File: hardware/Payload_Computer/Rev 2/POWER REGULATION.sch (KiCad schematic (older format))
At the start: 8 parts, among them U301 MIC29151-5.0WU-TR

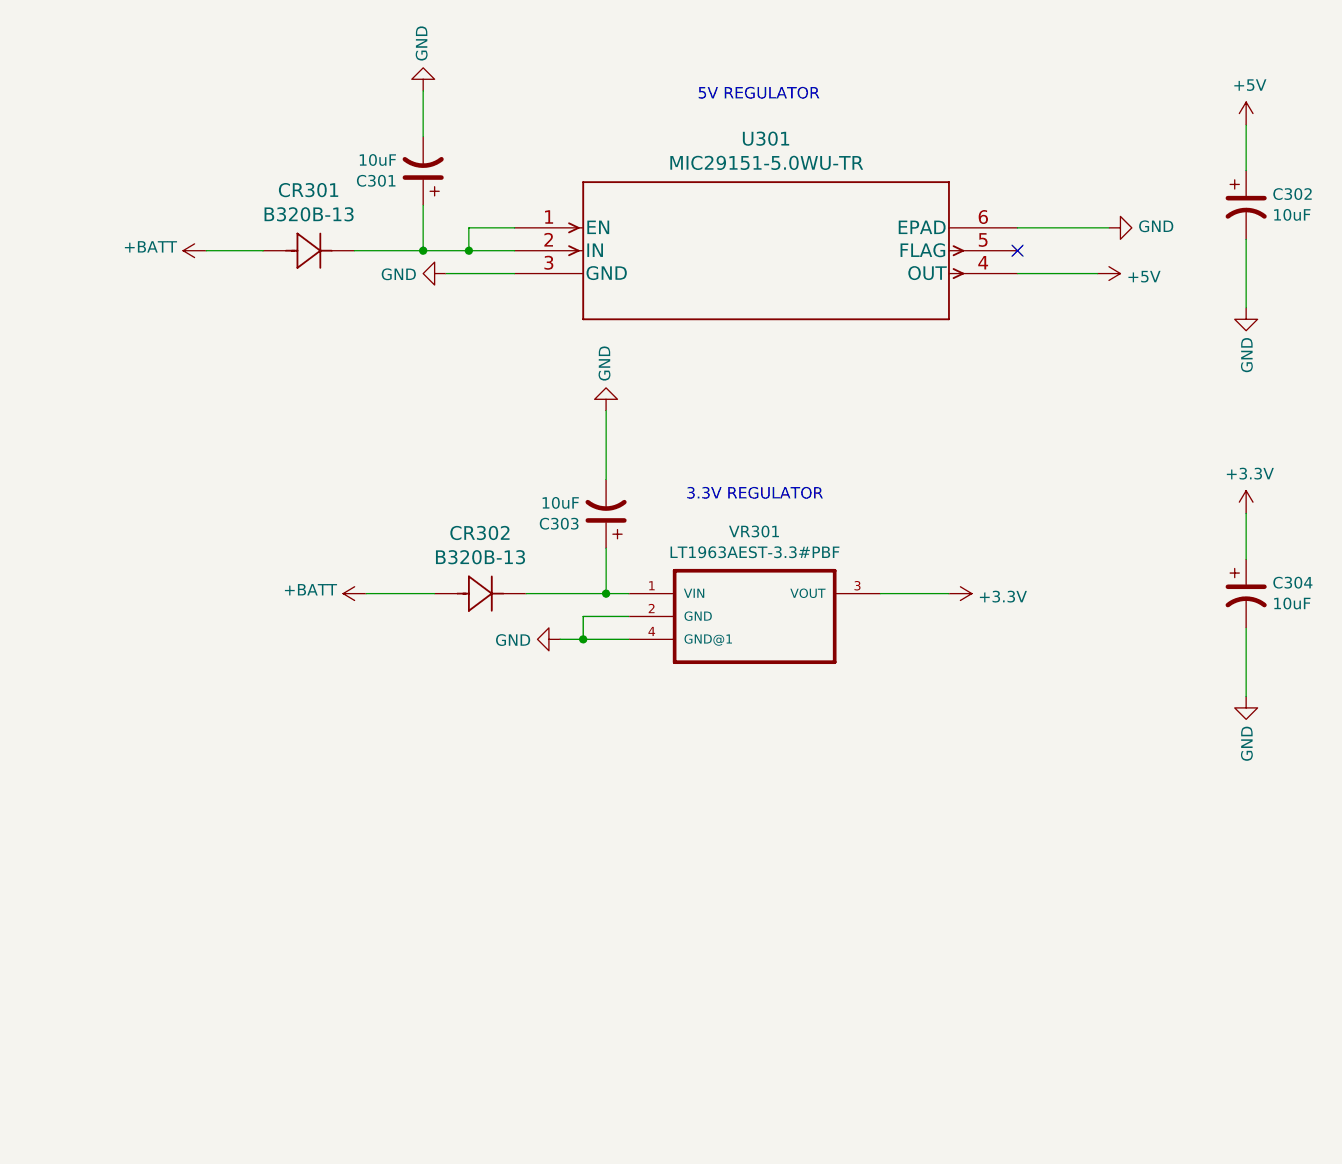
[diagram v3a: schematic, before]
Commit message: More routing and added BNO055
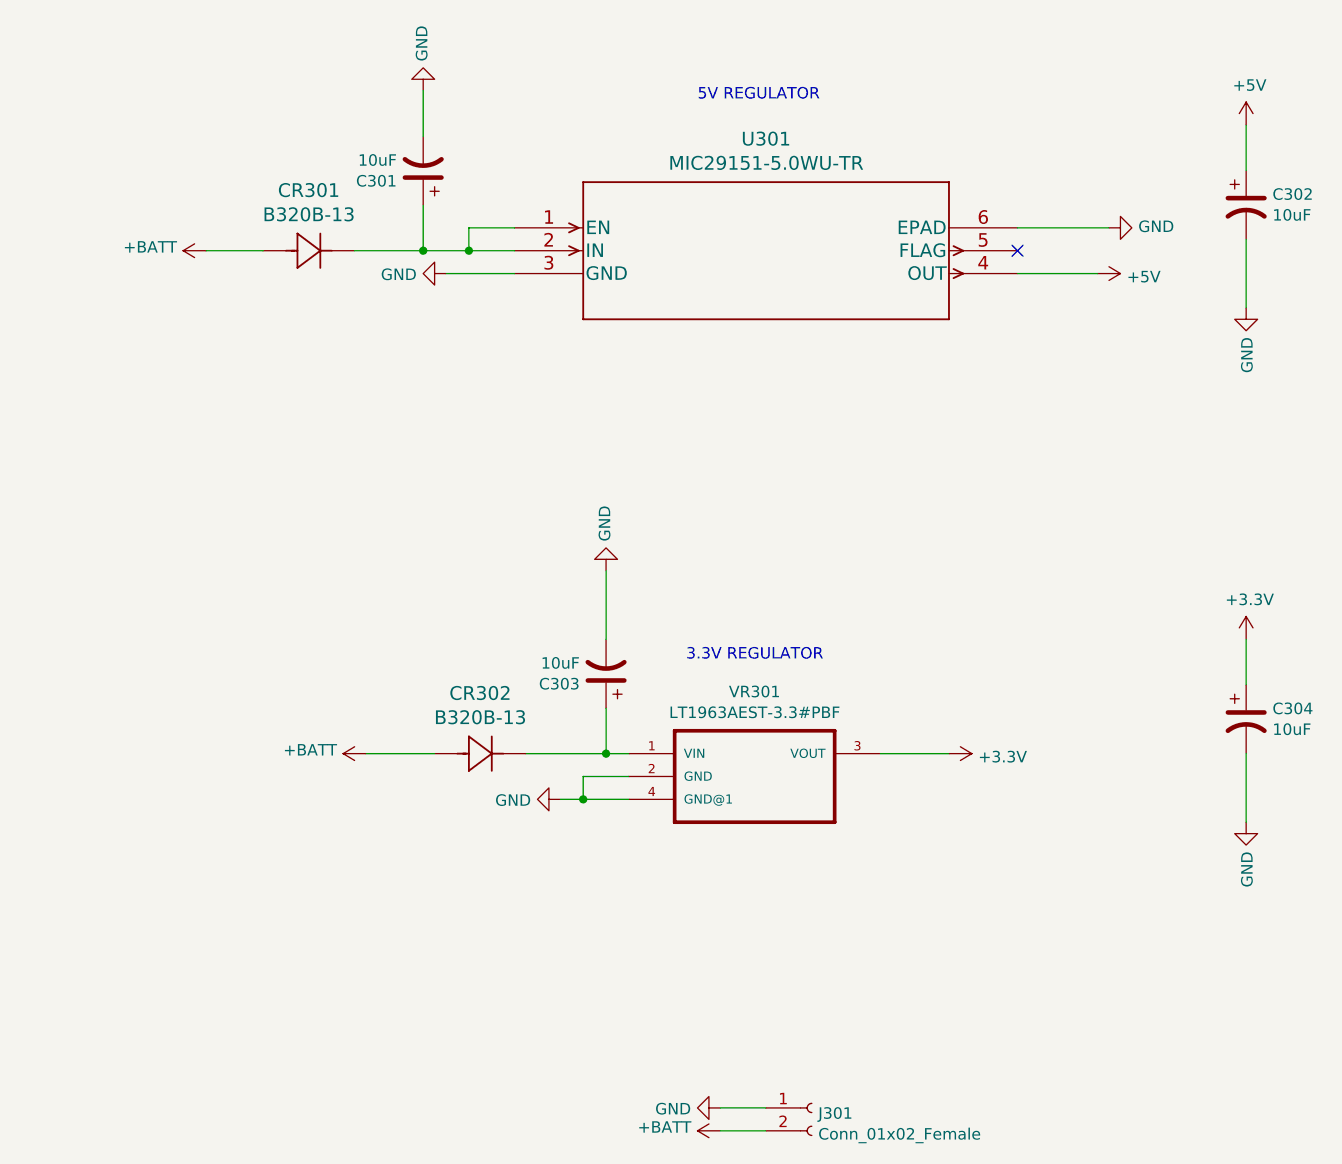
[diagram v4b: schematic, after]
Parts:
- added J301: Conn_01x02_Female, Connector_AMASS:AMASS_XT30PW-M_1x02_P2.50mm_Horizontal, symbol Connector:Conn_01x02_Female
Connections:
- net +BATT: now also J301.2 (Pin_2)
- net GND: now also J301.1 (Pin_1)
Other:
- moved on the sheet: C303, C304, CR302, VR301
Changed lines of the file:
@@
 $Descr A4 11693 8268
 encoding utf-8
-Sheet 3 3
+Sheet 3 5
 Title ""
 Date ""
@@
 L LT1963AEST-3.3_PBF:LT1963AEST-3.3#PBF VR301
 U 1 1 605971F7
-P 5400 3300
-F 0 "VR301" H 5750 3870 50  0000 C CNN
-F 1 "LT1963AEST-3.3#PBF" H 5750 3779 50  0000 C CNN
-F 2 "LT1963AEST-3:SOT223" H 5400 3300 50  0001 L BNN
-F 3 "" H 5400 3300 50  0001 L BNN
-F 4 "LT1963AEST-3.3#PBF" H 5400 3300 50  0001 L BNN "MPN"
-F 5 "No" H 5400 3300 50  0001 L BNN "MANUFACTURER"
-F 6 "LT1963AEST-3.3#PBF-ND" H 5400 3300 50  0001 C CNN "Digikey"
-	1    5400 3300
+P 5400 4000
+F 0 "VR301" H 5750 4570 50  0000 C CNN
+F 1 "LT1963AEST-3.3#PBF" H 5750 4479 50  0000 C CNN
+F 2 "LT1963AEST-3:SOT223" H 5400 4000 50  0001 L BNN
+F 3 "" H 5400 4000 50  0001 L BNN
+F 4 "LT1963AEST-3.3#PBF" H 5400 4000 50  0001 L BNN "MPN"
+F 5 "No" H 5400 4000 50  0001 L BNN "MANUFACTURER"
+F 6 "LT1963AEST-3.3#PBF-ND" H 5400 4000 50  0001 C CNN "Digikey"
+	1    5400 4000
 	1    0    0    -1
 $EndComp
@@
 L power:+BATT #PWR0303
 U 1 1 60597F5E
-P 4050 3000
-F 0 "#PWR0303" H 4050 2850 50  0001 C CNN
-F 1 "+BATT" V 4065 3127 50  0000 L CNN
-F 2 "" H 4050 3000 50  0001 C CNN
-F 3 "" H 4050 3000 50  0001 C CNN
-	1    4050 3000
+P 4050 3700
+F 0 "#PWR0303" H 4050 3550 50  0001 C CNN
+F 1 "+BATT" V 4065 3827 50  0000 L CNN
+F 2 "" H 4050 3700 50  0001 C CNN
+F 3 "" H 4050 3700 50  0001 C CNN
+	1    4050 3700
 	0    -1   -1   0
 $EndComp
@@
 L power:GND #PWR0304
 U 1 1 60598D50
-P 4900 3200
-F 0 "#PWR0304" H 4900 2950 50  0001 C CNN
-F 1 "GND" V 4905 3072 50  0000 R CNN
-F 2 "" H 4900 3200 50  0001 C CNN
-F 3 "" H 4900 3200 50  0001 C CNN
-	1    4900 3200
-	0    1    1    0
-$EndComp
-Wire Wire Line
-	5200 3200 5000 3200
-Wire Wire Line
-	5200 3100 5000 3100
-Wire Wire Line
-	5000 3100 5000 3200
-Connection ~ 5000 3200
-Wire Wire Line
-	5000 3200 4900 3200
+P 4900 3900
+F 0 "#PWR0304" H 4900 3650 50  0001 C CNN
+F 1 "GND" V 4905 3772 50  0000 R CNN
+F 2 "" H 4900 3900 50  0001 C CNN
+F 3 "" H 4900 3900 50  0001 C CNN
+	1    4900 3900
+	0    1    1    0
+$EndComp
+Wire Wire Line
+	5200 3900 5000 3900
+Wire Wire Line
+	5200 3800 5000 3800
+Wire Wire Line
+	5000 3800 5000 3900
+Connection ~ 5000 3900
+Wire Wire Line
+	5000 3900 4900 3900
 $Comp
 L power:+3.3V #PWR0305
 U 1 1 60599C96
-P 6600 3000
-F 0 "#PWR0305" H 6600 2850 50  0001 C CNN
-F 1 "+3.3V" V 6615 3128 50  0000 L CNN
-F 2 "" H 6600 3000 50  0001 C CNN
-F 3 "" H 6600 3000 50  0001 C CNN
-	1    6600 3000
-	0    1    1    0
-$EndComp
-Wire Wire Line
-	6300 3000 6600 3000
+P 6600 3700
+F 0 "#PWR0305" H 6600 3550 50  0001 C CNN
+F 1 "+3.3V" V 6615 3828 50  0000 L CNN
+F 2 "" H 6600 3700 50  0001 C CNN
+F 3 "" H 6600 3700 50  0001 C CNN
+	1    6600 3700
+	0    1    1    0
+$EndComp
+Wire Wire Line
+	6300 3700 6600 3700
 Wire Wire Line
 	4000 1500 4300 1500
@@
 	3350 1500 3600 1500
 Wire Wire Line
-	5100 3000 5100 2800
-Wire Wire Line
-	5100 2200 5100 2500
+	5100 3700 5100 3500
+Wire Wire Line
+	5100 2900 5100 3200
 $Comp
 L power:GND #PWR0302
 U 1 1 6059D143
-P 5100 2200
-F 0 "#PWR0302" H 5100 1950 50  0001 C CNN
-F 1 "GND" V 5105 2072 50  0000 R CNN
-F 2 "" H 5100 2200 50  0001 C CNN
-F 3 "" H 5100 2200 50  0001 C CNN
-	1    5100 2200
+P 5100 2900
+F 0 "#PWR0302" H 5100 2650 50  0001 C CNN
+F 1 "GND" V 5105 2772 50  0000 R CNN
+F 2 "" H 5100 2900 50  0001 C CNN
+F 3 "" H 5100 2900 50  0001 C CNN
+	1    5100 2900
 	-1   0    0    1
 $EndComp
@@
 L Device:CP1 C303
 U 1 1 6059D14A
-P 5100 2650
-F 0 "C303" H 5215 2696 50  0000 L CNN
-F 1 "10uF" H 5215 2605 50  0000 L CNN
-F 2 "Capacitor_Tantalum_SMD:CP_EIA-6032-20_AVX-F_Pad2.25x2.35mm_HandSolder" H 5100 2650 50  0001 C CNN
-F 3 "https://www.vishay.com/docs/40002/293d.pdf" H 5100 2650 50  0001 C CNN
-F 4 "718-1958-1-ND" H 5100 2650 50  0001 C CNN "DIGIKEY"
-	1    5100 2650
+P 5100 3350
+F 0 "C303" H 5215 3396 50  0000 L CNN
+F 1 "10uF" H 5215 3305 50  0000 L CNN
+F 2 "Capacitor_Tantalum_SMD:CP_EIA-6032-20_AVX-F_Pad2.25x2.35mm_HandSolder" H 5100 3350 50  0001 C CNN
+F 3 "https://www.vishay.com/docs/40002/293d.pdf" H 5100 3350 50  0001 C CNN
+F 4 "718-1958-1-ND" H 5100 3350 50  0001 C CNN "DIGIKEY"
+	1    5100 3350
 	-1   0    0    1
 $EndComp
 Wire Wire Line
-	7900 2650 7900 2850
-Wire Wire Line
-	7900 3450 7900 3150
+	7900 3200 7900 3400
+Wire Wire Line
+	7900 4000 7900 3700
 $Comp
 L power:GND #PWR0307
 U 1 1 6059DE65
-P 7900 3450
-F 0 "#PWR0307" H 7900 3200 50  0001 C CNN
-F 1 "GND" V 7905 3322 50  0000 R CNN
-F 2 "" H 7900 3450 50  0001 C CNN
-F 3 "" H 7900 3450 50  0001 C CNN
-	1    7900 3450
+P 7900 4000
+F 0 "#PWR0307" H 7900 3750 50  0001 C CNN
+F 1 "GND" V 7905 3872 50  0000 R CNN
+F 2 "" H 7900 4000 50  0001 C CNN
+F 3 "" H 7900 4000 50  0001 C CNN
+	1    7900 4000
 	1    0    0    -1
 $EndComp
@@
 L Device:CP1 C304
 U 1 1 6059DE6C
-P 7900 3000
-F 0 "C304" H 8015 3046 50  0000 L CNN
-F 1 "10uF" H 8015 2955 50  0000 L CNN
-F 2 "Capacitor_Tantalum_SMD:CP_EIA-6032-20_AVX-F_Pad2.25x2.35mm_HandSolder" H 7900 3000 50  0001 C CNN
-F 3 "https://www.vishay.com/docs/40002/293d.pdf" H 7900 3000 50  0001 C CNN
-F 4 "718-1958-1-ND" H 7900 3000 50  0001 C CNN "DIGIKEY"
-	1    7900 3000
+P 7900 3550
+F 0 "C304" H 8015 3596 50  0000 L CNN
+F 1 "10uF" H 8015 3505 50  0000 L CNN
+F 2 "Capacitor_Tantalum_SMD:CP_EIA-6032-20_AVX-F_Pad2.25x2.35mm_HandSolder" H 7900 3550 50  0001 C CNN
+F 3 "https://www.vishay.com/docs/40002/293d.pdf" H 7900 3550 50  0001 C CNN
+F 4 "718-1958-1-ND" H 7900 3550 50  0001 C CNN "DIGIKEY"
+	1    7900 3550
 	1    0    0    -1
 $EndComp
@@
 L power:+3.3V #PWR0306
 U 1 1 6059E119
-P 7900 2650
-F 0 "#PWR0306" H 7900 2500 50  0001 C CNN
-F 1 "+3.3V" H 7915 2823 50  0000 C CNN
-F 2 "" H 7900 2650 50  0001 C CNN
-F 3 "" H 7900 2650 50  0001 C CNN
-	1    7900 2650
-	1    0    0    -1
-$EndComp
-Text Notes 5450 2600 0    50   ~ 0
+P 7900 3200
+F 0 "#PWR0306" H 7900 3050 50  0001 C CNN
+F 1 "+3.3V" H 7915 3373 50  0000 C CNN
+F 2 "" H 7900 3200 50  0001 C CNN
+F 3 "" H 7900 3200 50  0001 C CNN
+	1    7900 3200
+	1    0    0    -1
+$EndComp
+Text Notes 5450 3300 0    50   ~ 0
 3.3V REGULATOR\n
 $Comp
@@
 $EndComp
 Wire Wire Line
-	4050 3000 4350 3000
+	4050 3700 4350 3700
 $Comp
 L 2021-03-23_04-45-24:B320B-13 CR302
 U 1 1 605A362B
-P 4350 3000
-F 0 "CR302" H 4550 3263 60  0000 C CNN
-F 1 "B320B-13" H 4550 3157 60  0000 C CNN
-F 2 "footprints-diode:B320B-13" H 4550 2640 60  0001 C CNN
-F 3 "https://media.digikey.com/pdf/Data%20Sheets/Diodes%20PDFs/B320B-B360B_Rev10-2.pdf" H 4550 3157 60  0001 C CNN
-F 4 "B320B-FDICT-ND" H 4350 3000 50  0001 C CNN "DIGIKEY"
-	1    4350 3000
+P 4350 3700
+F 0 "CR302" H 4550 3963 60  0000 C CNN
+F 1 "B320B-13" H 4550 3857 60  0000 C CNN
+F 2 "footprints-diode:B320B-13" H 4550 3340 60  0001 C CNN
+F 3 "https://media.digikey.com/pdf/Data%20Sheets/Diodes%20PDFs/B320B-B360B_Rev10-2.pdf" H 4550 3857 60  0001 C CNN
+F 4 "B320B-FDICT-ND" H 4350 3700 50  0001 C CNN "DIGIKEY"
+	1    4350 3700
 	1    0    0    -1
 $EndComp
@@
 Wire Wire Line
 	4300 800  4300 1000
-Connection ~ 5100 3000
-Wire Wire Line
-	5100 3000 5200 3000
-Wire Wire Line
-	4750 3000 5100 3000
+Connection ~ 5100 3700
+Wire Wire Line
+	5100 3700 5200 3700
+Wire Wire Line
+	4750 3700 5100 3700
+$Comp
+L Connector:Conn_01x02_Female J301
+U 1 1 605FE663
+P 6000 5250
+F 0 "J301" H 6028 5226 50  0000 L CNN
+F 1 "Conn_01x02_Female" H 6028 5135 50  0000 L CNN
+F 2 "Connector_AMASS:AMASS_XT30PW-M_1x02_P2.50mm_Horizontal" H 6000 5250 50  0001 C CNN
+F 3 "~" H 6000 5250 50  0001 C CNN
+	1    6000 5250
+	1    0    0    -1
+$EndComp
+$Comp
+L power:+BATT #PWR0113
+U 1 1 605FFCFC
+P 5600 5350
+F 0 "#PWR0113" H 5600 5200 50  0001 C CNN
+F 1 "+BATT" V 5615 5477 50  0000 L CNN
+F 2 "" H 5600 5350 50  0001 C CNN
+F 3 "" H 5600 5350 50  0001 C CNN
+	1    5600 5350
+	0    -1   -1   0
+$EndComp
+Wire Wire Line
+	5600 5350 5800 5350
+$Comp
+L power:GND #PWR0114
+U 1 1 60600C1E
+P 5600 5250
+F 0 "#PWR0114" H 5600 5000 50  0001 C CNN
+F 1 "GND" V 5605 5122 50  0000 R CNN
+F 2 "" H 5600 5250 50  0001 C CNN
+F 3 "" H 5600 5250 50  0001 C CNN
+	1    5600 5250
+	0    1    1    0
+$EndComp
+Wire Wire Line
+	5600 5250 5800 5250
 $EndSCHEMATC
